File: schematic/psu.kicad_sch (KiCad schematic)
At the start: 0 parts

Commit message: power supply added, controller circuit added. Controller is a very odd duck to say the least. Seems they wanted to have plenty of current, maybe due to the steering wheel attachement?
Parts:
- added C34: 10uF, symbol Device:C_Polarized
- added C41, C46, C47, C48, C49, C50, C51: 100nF, symbol Device:C
- added L2, L3, L4: 10uH, symbol Device:L
- added L5, L6: 12uH, symbol Device:L
- added S2: SW_DPDT_x2, symbol Switch:SW_DPDT_x2
- added WJ2: Jumper_2_Bridged, symbol Jumper:Jumper_2_Bridged
- added WJ3: Jumper_2_Open, symbol Jumper:Jumper_2_Open
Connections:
- new net: L6.1, S2.3 (C)
- new net: L5.1, S2.6 (C)
- new net +12C: C47.2, S2.4 (A), S2.5 (B)
- new net +12V: L3.2
- new net +12VL: C50.2, L3.1, L5.2, WJ2.1 (A)
- new net +5C: C48.2, S2.1 (A), S2.2 (B)
- new net +5V: C51.1, L6.2, WJ3.2 (B)
- new net -5C: C46.2, L4.1
- new net -5V: C34.2, C41.2, L2.2
- new net -5VL: C49.2, L2.1, L4.2
- new net GNDD: C34.1, C41.1, C46.1, C47.1, C48.1, C49.1, C50.1, C51.2
- new net VDDA: WJ2.2 (B), WJ3.1 (A)

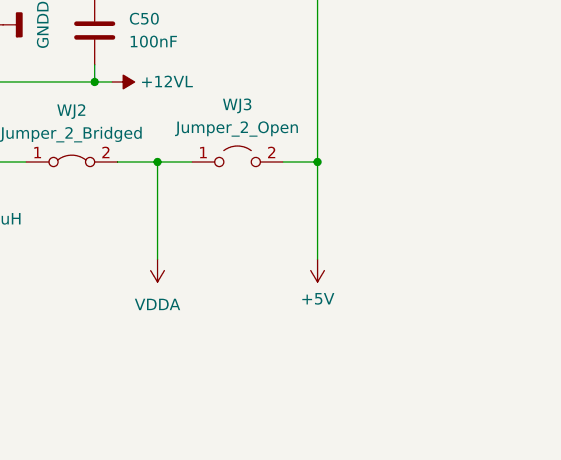
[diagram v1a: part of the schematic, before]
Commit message: first version of clock-reset circuits. Its a bit complicated and will need some revisions.
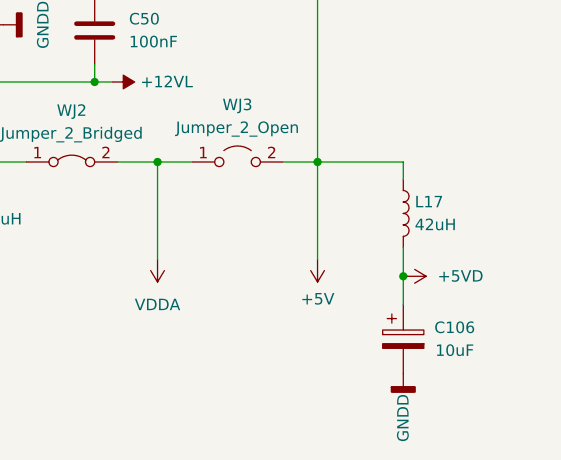
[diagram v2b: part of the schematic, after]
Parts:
- added C106: 10uF, symbol Device:C_Polarized
- added L17: 42uH, symbol Device:L
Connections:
- net +5V: now also L17.1
- net GNDD: now also C106.2
- new net +5VD: C106.1, L17.2
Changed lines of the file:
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@@
   (junction (at 113.665 80.01) (diameter 0) (color 0 0 0 0)
   )
+  (junction (at 182.88 122.555) (diameter 0) (color 0 0 0 0)
+  )
   (junction (at 179.07 61.595) (diameter 0) (color 0 0 0 0)
   )
@@
     (stroke (width 0) (type default) (color 0 0 0 0))
   )
+  (wire (pts (xy 182.88 109.855) (xy 182.88 111.76))
+    (stroke (width 0) (type default) (color 0 0 0 0))
+  )
+  (wire (pts (xy 182.88 122.555) (xy 182.88 125.73))
+    (stroke (width 0) (type default) (color 0 0 0 0))
+  )
   (wire (pts (xy 134.62 118.745) (xy 134.62 120.65))
     (stroke (width 0) (type default) (color 0 0 0 0))
@@
   )
   (wire (pts (xy 123.825 95.885) (xy 123.825 94.615))
+    (stroke (width 0) (type default) (color 0 0 0 0))
+  )
+  (wire (pts (xy 182.88 119.38) (xy 182.88 122.555))
+    (stroke (width 0) (type default) (color 0 0 0 0))
+  )
+  (wire (pts (xy 173.355 109.855) (xy 182.88 109.855))
     (stroke (width 0) (type default) (color 0 0 0 0))
   )
@@
     (pin "1")
   )
+  (symbol (lib_id "Device:C_Polarized") (at 182.88 129.54 0) (unit 1)
+    (in_bom yes) (on_board yes)
+    (property "Reference" "C106" (id 0) (at 188.595 128.27 0))
+    (property "Value" "10uF" (id 1) (at 188.595 130.81 0))
+    (property "Footprint" "" (id 2) (at 183.8452 133.35 0)
+      (effects (font (size 1.27 1.27)) hide)
+    )
+    (property "Datasheet" "~" (id 3) (at 182.88 129.54 0)
+      (effects (font (size 1.27 1.27)) hide)
+    )
+    (pin "1")
+    (pin "2")
+  )
   (symbol (lib_id "power:GNDD") (at 179.07 52.07 180) (unit 1)
     (in_bom yes) (on_board yes) (fields_autoplaced)
@@
     (pin "6")
   )
+  (symbol (lib_id "power:GNDD") (at 182.88 133.35 0) (unit 1)
+    (in_bom yes) (on_board yes)
+    (property "Reference" "#PWR?" (id 0) (at 182.88 139.7 0)
+      (effects (font (size 1.27 1.27)) hide)
+    )
+    (property "Value" "GNDD" (id 1) (at 182.88 140.97 90)
+      (effects (font (size 1.27 1.27)) (justify left))
+    )
+    (property "Footprint" "" (id 2) (at 182.88 133.35 0)
+      (effects (font (size 1.27 1.27)) hide)
+    )
+    (property "Datasheet" "" (id 3) (at 182.88 133.35 0)
+      (effects (font (size 1.27 1.27)) hide)
+    )
+    (pin "1")
+  )
   (symbol (lib_id "power:GNDD") (at 166.37 52.07 180) (unit 1)
     (in_bom yes) (on_board yes) (fields_autoplaced)
@@
       (effects (font (size 1.27 1.27)) hide)
     )
+    (pin "1")
+    (pin "2")
+  )
+  (symbol (lib_id "power:+5VD") (at 182.88 122.555 270) (unit 1)
+    (in_bom yes) (on_board yes) (fields_autoplaced)
+    (property "Reference" "#PWR?" (id 0) (at 179.07 122.555 0)
+      (effects (font (size 1.27 1.27)) hide)
+    )
+    (property "Value" "+5VD" (id 1) (at 186.69 122.5549 90)
+      (effects (font (size 1.27 1.27)) (justify left))
+    )
+    (property "Footprint" "" (id 2) (at 182.88 122.555 0)
+      (effects (font (size 1.27 1.27)) hide)
+    )
+    (property "Datasheet" "" (id 3) (at 182.88 122.555 0)
+      (effects (font (size 1.27 1.27)) hide)
+    )
+    (pin "1")
+  )
+  (symbol (lib_id "Device:L") (at 182.88 115.57 0) (unit 1)
+    (in_bom yes) (on_board yes) (fields_autoplaced)
+    (property "Reference" "L17" (id 0) (at 184.15 114.2999 0)
+      (effects (font (size 1.27 1.27)) (justify left))
+    )
+    (property "Value" "42uH" (id 1) (at 184.15 116.8399 0)
+      (effects (font (size 1.27 1.27)) (justify left))
+    )
+    (property "Footprint" "" (id 2) (at 182.88 115.57 0)
+      (effects (font (size 1.27 1.27)) hide)
+    )
+    (property "Datasheet" "~" (id 3) (at 182.88 115.57 0)
+      (effects (font (size 1.27 1.27)) hide)
+    )

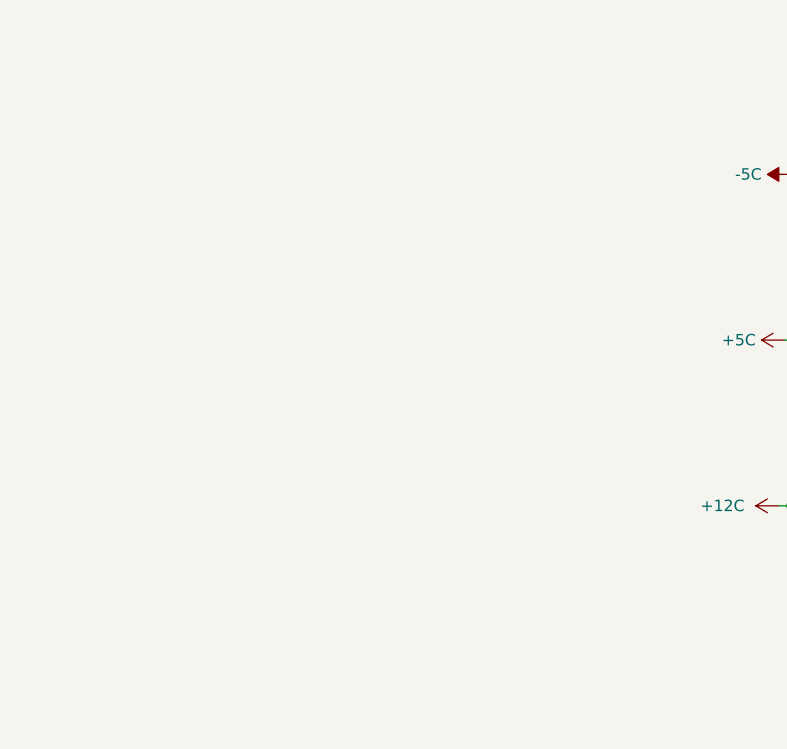
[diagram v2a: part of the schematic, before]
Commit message: altered and did some cleanup of the way the wires were run. Finished expansion port routes to rf modulator. Added ext_psu for future external power supply design (will be an off the shelf psu block).
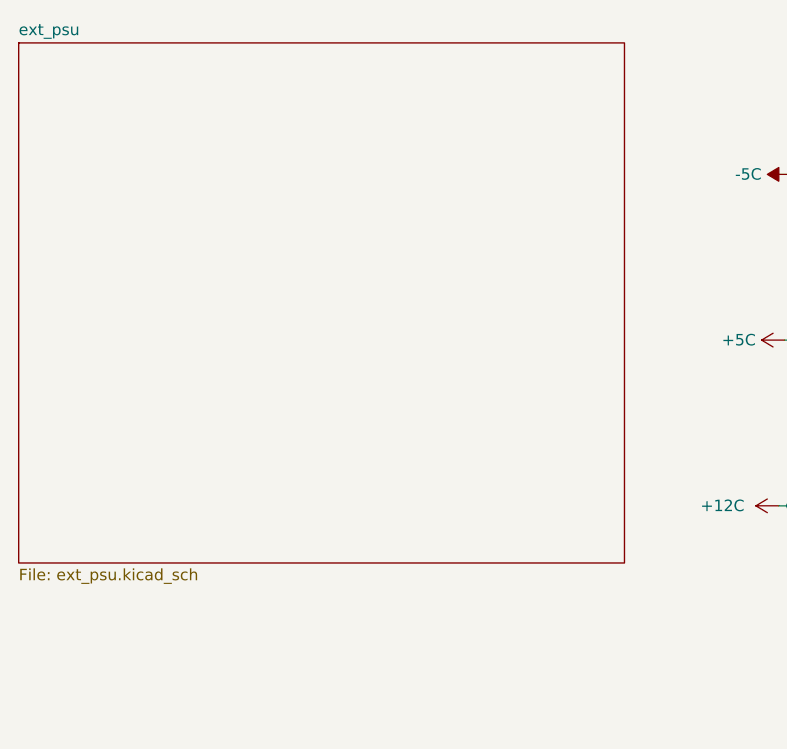
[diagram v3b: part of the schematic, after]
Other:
- added sheet ext_psu (ext_psu.kicad_sch)
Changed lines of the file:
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@@
     (pin "1")
   )
+  (sheet (at 27.305 46.99) (size 67.31 57.785) (fields_autoplaced)
+    (stroke (width 0.1524) (type solid) (color 0 0 0 0))
+    (fill (color 0 0 0 0.0000))
+    (property "Sheet name" "ext_psu" (id 0) (at 27.305 46.2784 0)
+      (effects (font (size 1.27 1.27)) (justify left bottom))
+    )
+    (property "Sheet file" "ext_psu.kicad_sch" (id 1) (at 27.305 105.3596 0)
+      (effects (font (size 1.27 1.27)) (justify left top))
+    )
+  )
 )

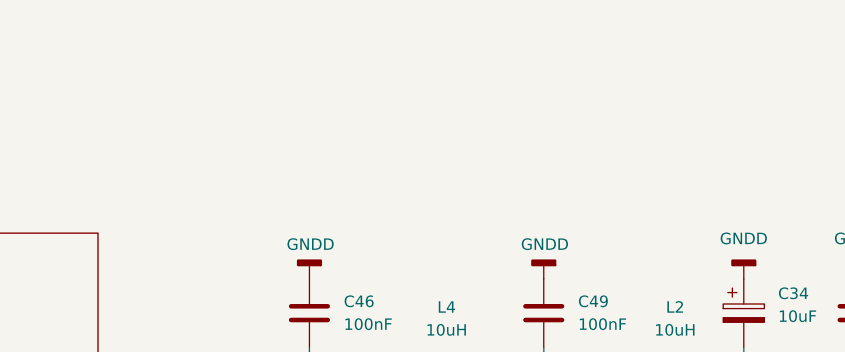
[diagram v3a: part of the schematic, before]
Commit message: RF modulator completed, rough draft complete. Next step is to clean-up all pages.
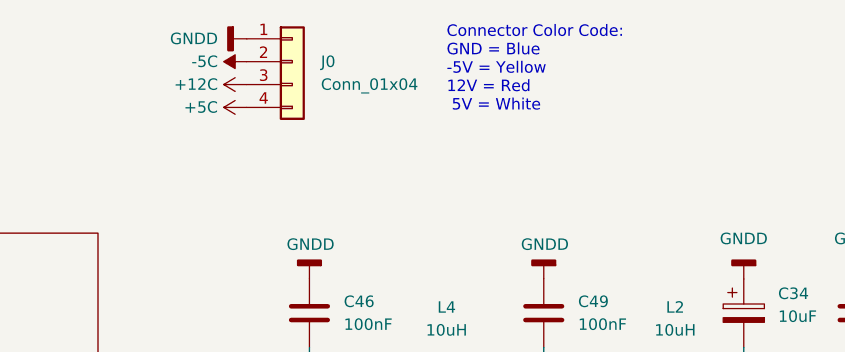
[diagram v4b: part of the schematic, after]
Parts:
- added J0: Conn_01x04, symbol Connector_Generic:Conn_01x04
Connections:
- net +12C: now also J0.3 (Pin_3)
- net +5C: now also J0.4 (Pin_4)
- net -5C: now also J0.2 (Pin_2)
- net GNDD: now also J0.1 (Pin_1)
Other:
- note added: "Connector Color Code: GND = Blue -5V = Yellow 12V = Red 5V = White"
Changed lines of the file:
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@@
     (stroke (width 0) (type default) (color 0 0 0 0))
+  )
+  (text "Connector Color Code:\nGND = Blue\n-5V = Yellow\n12V = Red\n 5V = White"
+    (at 133.35 33.655 0)
+    (effects (font (size 1.27 1.27)) (justify left bottom))
   )
   (symbol (lib_id "Device:L") (at 130.175 82.55 90) (unit 1)
@@
     (pin "1")
     (pin "2")
+  )
+  (symbol (lib_id "power:+12C") (at 111.125 30.48 90) (unit 1)
+    (in_bom yes) (on_board yes)
+    (property "Reference" "#PWR?" (id 0) (at 114.935 30.48 0)
+      (effects (font (size 1.27 1.27)) hide)
+    )
+    (property "Value" "+12C" (id 1) (at 107.95 30.48 90)
+      (effects (font (size 1.27 1.27)) (justify left))
+    )
+    (property "Footprint" "" (id 2) (at 111.125 30.48 0)
+      (effects (font (size 1.27 1.27)) hide)
+    )
+    (property "Datasheet" "" (id 3) (at 111.125 30.48 0)
+      (effects (font (size 1.27 1.27)) hide)
+    )
+    (pin "1")
   )
   (symbol (lib_id "power:VDDA") (at 155.575 120.65 180) (unit 1)
@@
     (pin "2")
   )
+  (symbol (lib_id "power:+5C") (at 111.125 33.02 90) (unit 1)
+    (in_bom yes) (on_board yes)
+    (property "Reference" "#PWR?" (id 0) (at 114.935 33.02 0)
+      (effects (font (size 1.27 1.27)) hide)
+    )
+    (property "Value" "+5C" (id 1) (at 106.045 33.02 90))
+    (property "Footprint" "" (id 2) (at 111.125 33.02 0)
+      (effects (font (size 1.27 1.27)) hide)
+    )
+    (property "Datasheet" "" (id 3) (at 111.125 33.02 0)
+      (effects (font (size 1.27 1.27)) hide)
+    )
+    (pin "1")
+  )
   (symbol (lib_id "power:GNDD") (at 179.07 52.07 180) (unit 1)
     (in_bom yes) (on_board yes) (fields_autoplaced)
@@
     (pin "1")
     (pin "2")
+  )
+  (symbol (lib_id "power:GNDD") (at 111.125 25.4 270) (unit 1)
+    (in_bom yes) (on_board yes)
+    (property "Reference" "#PWR?" (id 0) (at 104.775 25.4 0)
+      (effects (font (size 1.27 1.27)) hide)
+    )
+    (property "Value" "GNDD" (id 1) (at 107.95 25.4 90)
+      (effects (font (size 1.27 1.27)) (justify right))
+    )
+    (property "Footprint" "" (id 2) (at 111.125 25.4 0)
+      (effects (font (size 1.27 1.27)) hide)
+    )
+    (property "Datasheet" "" (id 3) (at 111.125 25.4 0)
+      (effects (font (size 1.27 1.27)) hide)
+    )
+    (pin "1")
   )
   (symbol (lib_id "Device:C") (at 118.11 55.88 0) (unit 1)
@@
     (pin "1")
   )
+  (symbol (lib_id "Connector_Generic:Conn_01x04") (at 116.205 27.94 0) (unit 1)
+    (in_bom yes) (on_board yes) (fields_autoplaced)
+    (property "Reference" "J0" (id 0) (at 119.38 27.9399 0)
+      (effects (font (size 1.27 1.27)) (justify left))
+    )
+    (property "Value" "Conn_01x04" (id 1) (at 119.38 30.4799 0)
+      (effects (font (size 1.27 1.27)) (justify left))
+    )
+    (property "Footprint" "" (id 2) (at 116.205 27.94 0)
+      (effects (font (size 1.27 1.27)) hide)
+    )
+    (property "Datasheet" "~" (id 3) (at 116.205 27.94 0)
+      (effects (font (size 1.27 1.27)) hide)
+    )
+    (pin "1")
+    (pin "2")
+    (pin "3")
+    (pin "4")
+  )
   (symbol (lib_id "power:-5V") (at 190.5 61.595 270) (unit 1)
     (in_bom yes) (on_board yes) (fields_autoplaced)
@@
       (effects (font (size 1.27 1.27)) hide)
     )
+    (pin "1")
+  )
+  (symbol (lib_id "Power_Symbols:-5C") (at 111.125 27.94 90) (unit 1)
+    (in_bom yes) (on_board yes) (fields_autoplaced)
+    (property "Reference" "#PWR?" (id 0) (at 108.585 27.94 0)
+      (effects (font (size 1.27 1.27)) hide)
+    )
+    (property "Value" "-5C" (id 1) (at 107.95 27.9399 90)
+      (effects (font (size 1.27 1.27)) (justify left))
+    )
+    (property "Footprint" "" (id 2) (at 111.125 27.94 0)
+      (effects (font (size 1.27 1.27)) hide)
+    )
+    (property "Datasheet" "" (id 3) (at 111.125 27.94 0)
+      (effects (font (size 1.27 1.27)) hide)
+    )

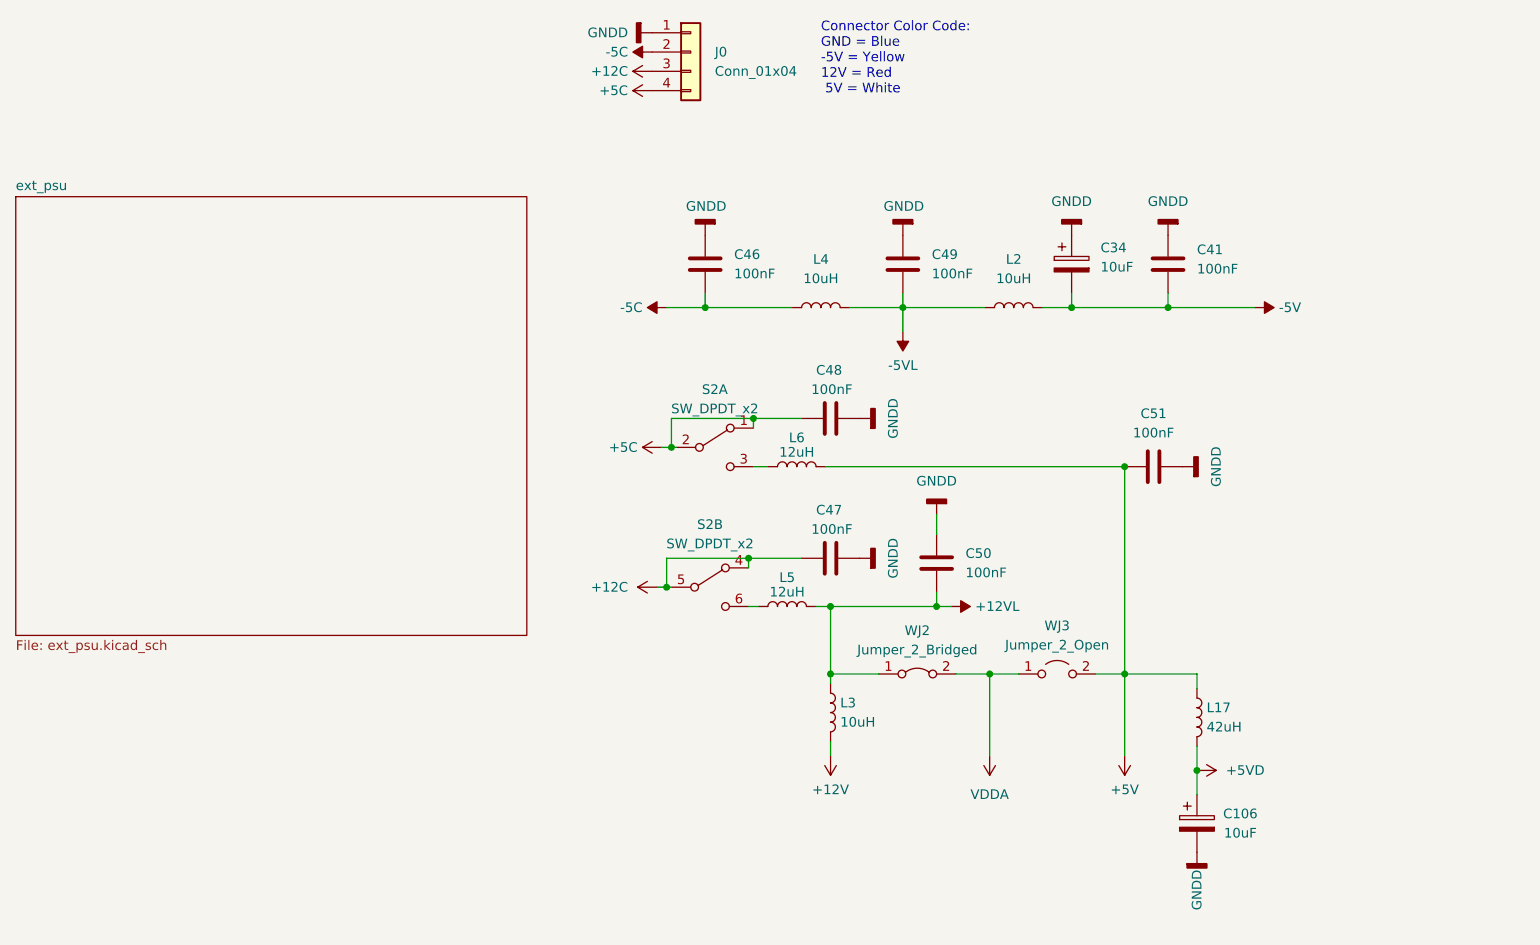
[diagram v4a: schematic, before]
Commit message: cleanup of power supply, and another pass at the RF circuit. Both look much better. The RF circuit just looks wrong though. Will need to check it over.
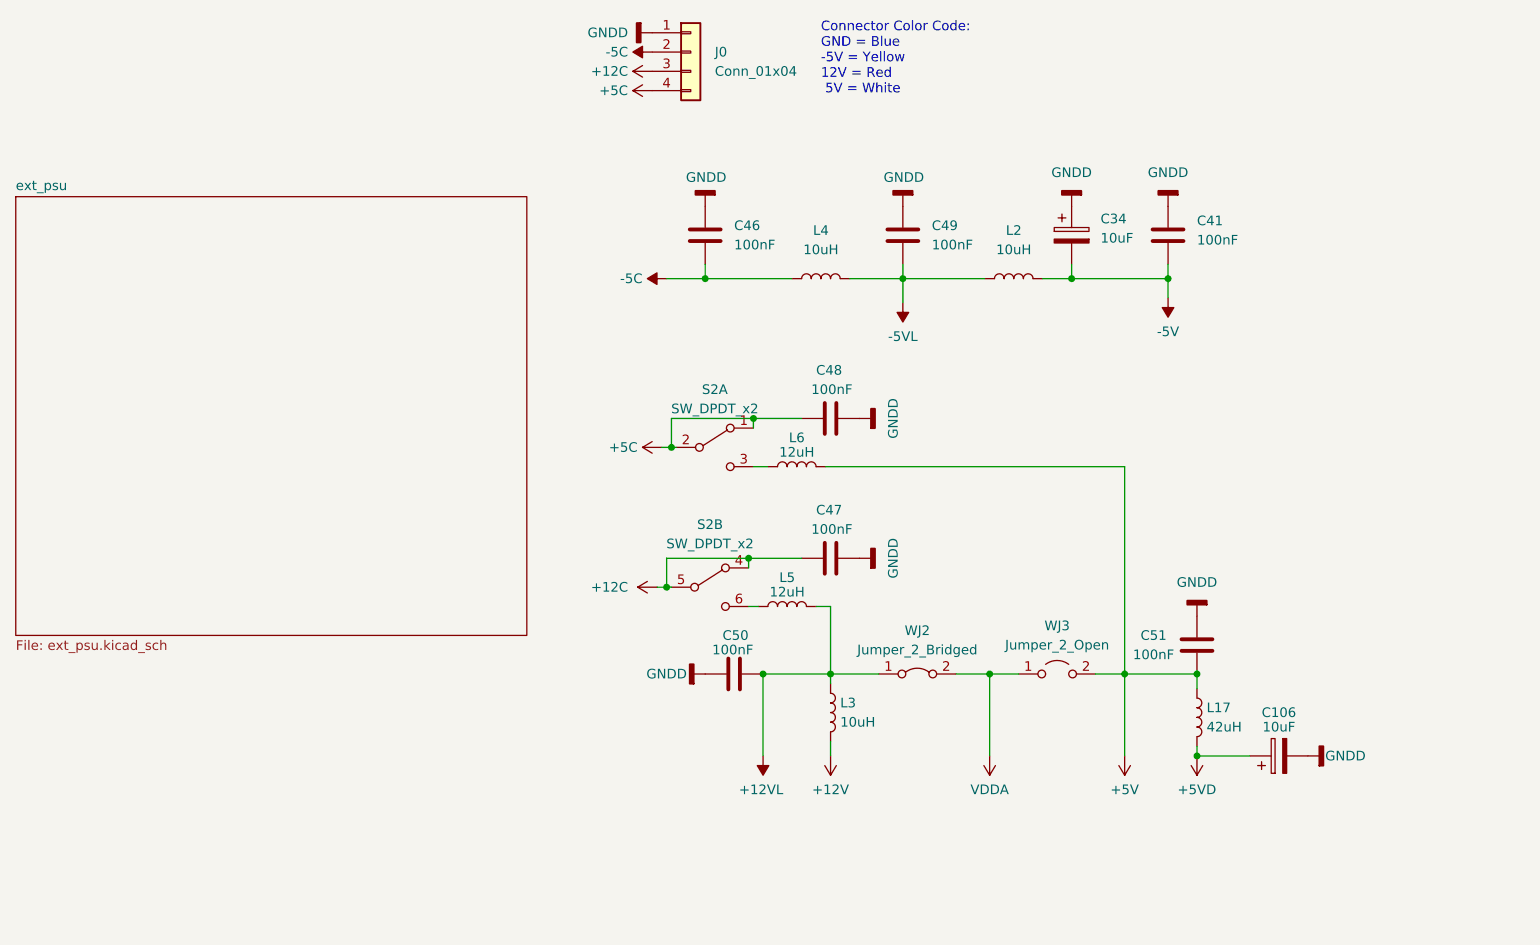
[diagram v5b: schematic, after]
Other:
- moved on the sheet: C106, C34, C41, C46, C49, C50, C51, L2, L4
